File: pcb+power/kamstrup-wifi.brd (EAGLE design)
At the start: 36 x 81.3 mm, 23 parts, among them T1 BT137, T2 BT137

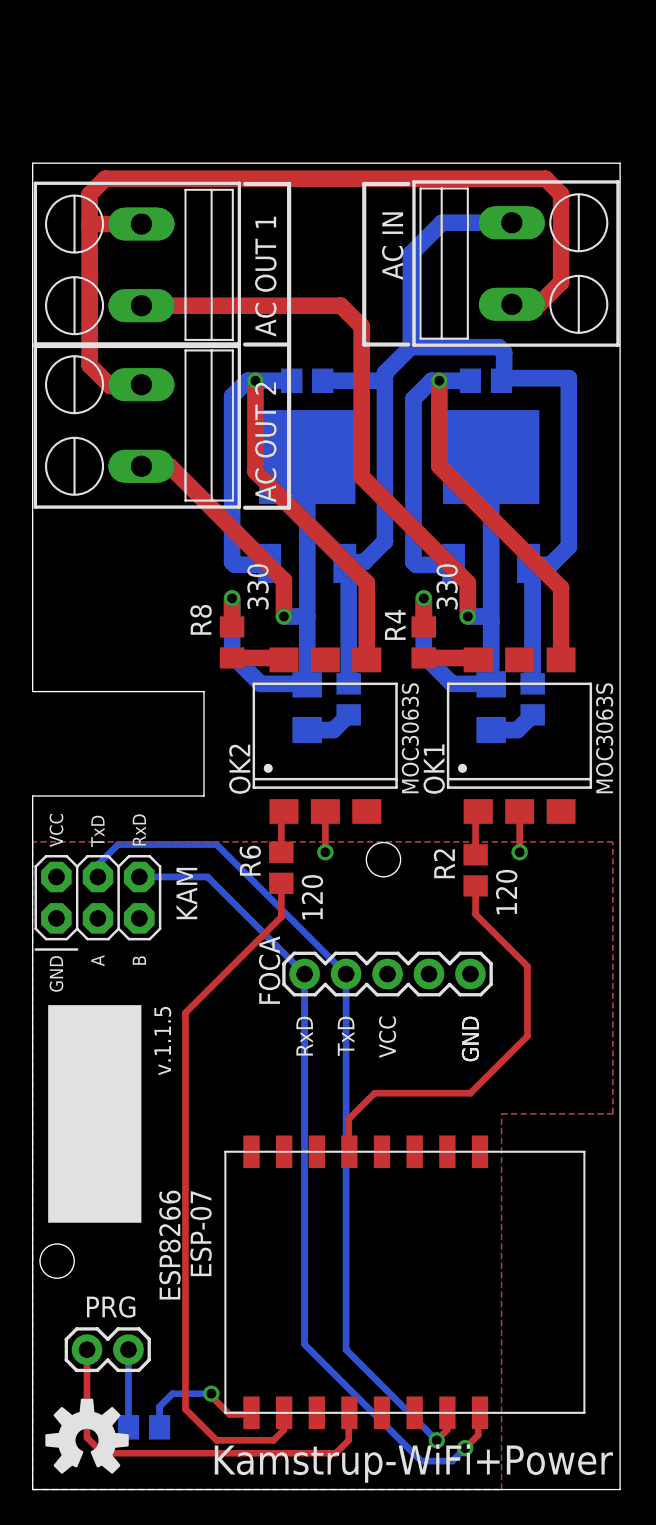
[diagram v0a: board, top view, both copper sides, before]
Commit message: v.1.2.1
+ watchdog and pulldown on gpio 15
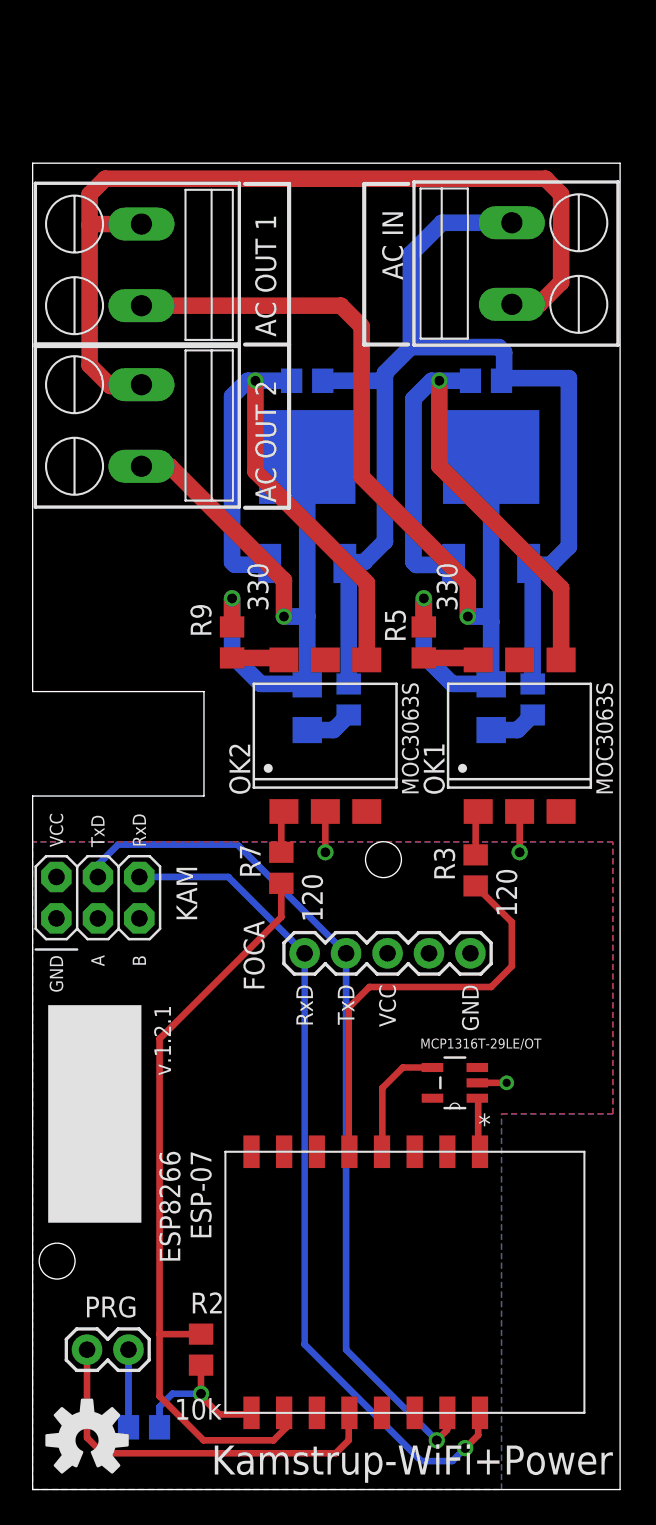
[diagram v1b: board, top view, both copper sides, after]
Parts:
- added R10: 39, rcl:R0805
- added U2: MCP1316T-29LE/OT, Microchip_By_element14_Batch_1:SOT95P270X145-5N
- R2: value 120 -> 10k
- R3, R7: value 330 -> 120
- R5, R9: value 39 -> 330
- R6: value 120 -> 39
- moved R2 33.8 mm to (10.3, 8.57)
- moved R3 30.0 mm to (27.1, 37.9), flipped to the top, turned to 90 degrees
- moved R7 29.9 mm to (15.2, 38.1), flipped to the top, turned to 90 degrees
- moved R6 18.5 mm to (30.6, 48.4), flipped to the bottom, turned to 270 degrees
- moved R8 16.7 mm to (16.8, 67.9), flipped to the bottom, turned to 180 degrees
- moved R4 16.5 mm to (27.8, 67.9), flipped to the bottom, turned to 180 degrees
- moved R9 7.95 mm to (12.2, 51.9), flipped to the top, turned to 90 degrees
- moved R5 7.53 mm to (24.0, 51.9), flipped to the top, turned to 90 degrees
- moved FOCA 1.27 mm to (16.7, 32.9)
- renumbered U$1 to U1
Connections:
- new net N$19: U1.REST, U2.1
- new net N$20: U1.GPIO16, U2.4
- net 3.3V: now also U2.5
- net GND: now also R2.1, U2.2
- net N$10: now also R10.2; no longer R9.2
- net N$11: now also R3.1; no longer R2.1
- net N$12: now also R3.2; no longer R2.2
- net N$13: now also R4.1; no longer R3.1
- net N$14: now also R5.1; no longer R4.1
- net N$15: now also R5.2; no longer R4.2
- net N$16: now also R2.2, R7.1; no longer R6.1
- net N$17: now also R6.2; no longer R5.2
- net N$5: now also R7.2; no longer R6.2
- net N$6: now also R8.1; no longer R7.1
- net N$7: now also R9.1; no longer R8.1
- net N$8: now also R9.2; no longer R8.2
- net N$9: now also R10.1, R4.2, R6.1, R8.2; no longer R3.2, R5.1, R7.2, R9.1
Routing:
- net N$20: track 0.00 -> 7.51 mm
- net N$16: track 42.8 -> 47.3 mm
- net GND: track 14.2 -> 17.8 mm, vias 3 -> 4
- net N$19: track 0.00 -> 3.35 mm
- net N$2: track 52.6 -> 53.3 mm
- net N$1: track 51.0 -> 51.7 mm
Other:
- board text added: "Part RS# C1, C2 766-1150 JP1, JP2, JP3 821-8701 KAM 702-2937 OK1, OK2 691-2319 R1, R2 721-7820 R3, R7 721-6867 R4, R5, R8, R9 770-8742 R6, R10 770-8798 T1, T2 792-0709"
- board text added: "v.1.2.1"
- board text removed: "Part RS# C1, C2 766-1150 JP1, JP2, JP3 821-8701 KAM 702-2937 OK1, OK2 691-2319 R1 721-7820 R2, R6 721-6867 R3, R4, R7, R8 770-8742 R5, R9 770-8798 T1, T2 792-0709"
- board text removed: "v.1.1.5"

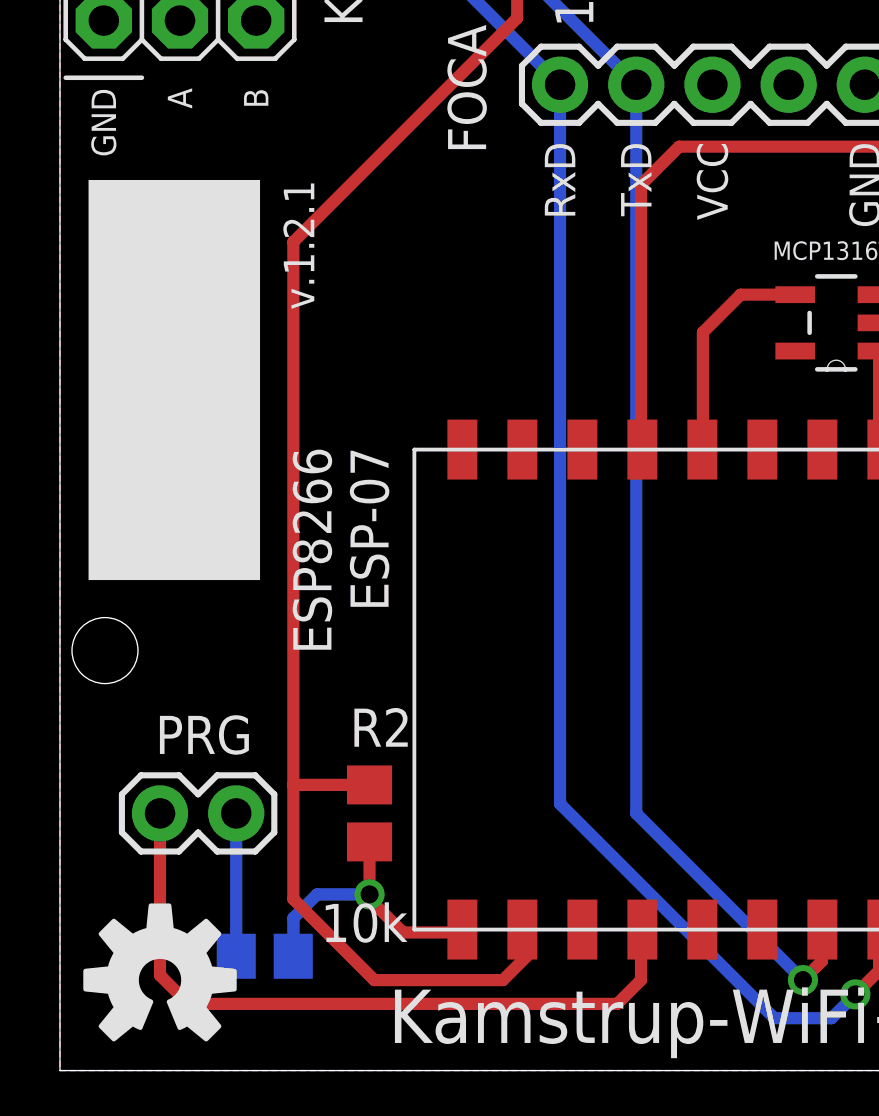
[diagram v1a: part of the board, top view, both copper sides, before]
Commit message: added pull up resistor on GPIO02
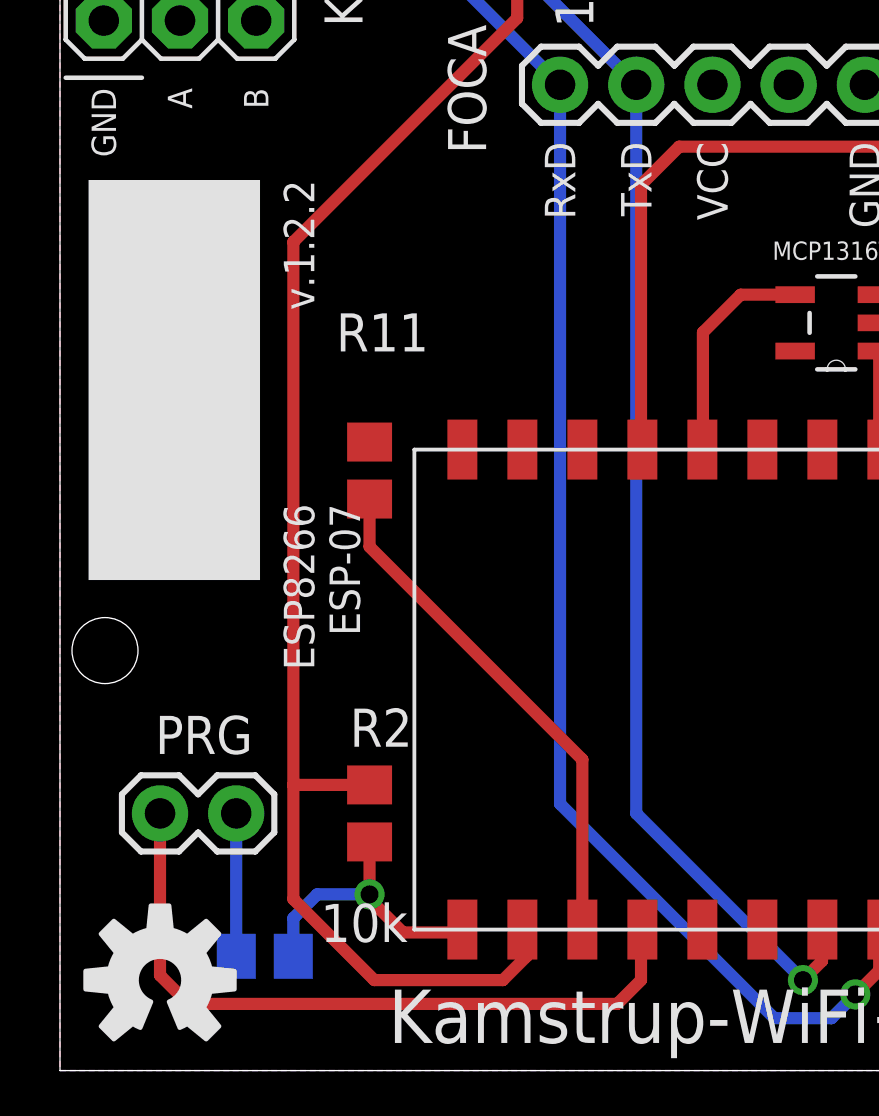
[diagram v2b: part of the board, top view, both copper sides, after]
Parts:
- added R11: 10k, rcl:R0805
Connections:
- new net N$21: R11.2, U1.GPIO2
- net 3.3V: now also R11.1
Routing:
- net N$21: track 0.00 -> 17.3 mm
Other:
- board text added: "Part RS# C1, C2 766-1150 JP1, JP2, JP3 821-8701 KAM 702-2937 OK1, OK2 691-2319 R1, R2, R11 721-7820 R3, R7 721-6867 R4, R5, R8, R9 770-8742 R6, R10 770-8798 T1, T2 792-0709"
- board text added: "v.1.2.2"
- board text removed: "Part RS# C1, C2 766-1150 JP1, JP2, JP3 821-8701 KAM 702-2937 OK1, OK2 691-2319 R1, R2 721-7820 R3, R7 721-6867 R4, R5, R8, R9 770-8742 R6, R10 770-8798 T1, T2 792-0709"
- board text removed: "v.1.2.1"
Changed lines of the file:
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@@
 <?xml version="1.0" encoding="utf-8"?>
 <!DOCTYPE eagle SYSTEM "eagle.dtd">
-<eagle version="7.2.0">
+<eagle version="7.6.0">
 <drawing>
 <settings>
@@
 <setting verticaltext="up"/>
 </settings>
-<grid distance="0.00625" unitdist="inch" unit="mm" style="dots" multiple="1" display="no" altdistance="0.0125" altunitdist="inch" altunit="mm"/>
+<grid distance="0.00625" unitdist="inch" unit="inch" style="dots" multiple="1" display="no" altdistance="0.0125" altunitdist="inch" altunit="inch"/>
 <layers>
 <layer number="1" name="Top" color="4" fill="1" visible="yes" active="yes"/>
@@
 <text x="19.20875" y="30.95625" size="1.016" layer="25" rot="R90" align="center-right">TxD</text>
 <text x="16.66875" y="30.95625" size="1.016" layer="25" rot="R90" align="center-right">RxD</text>
-<text x="7.77875" y="20.79625" size="1.27" layer="25" ratio="10" rot="R270">ESP8266
+<text x="7.46125" y="18.89125" size="1.016" layer="25" ratio="10" rot="R270">ESP8266
 ESP-07</text>
-<text x="7.46125" y="29.68625" size="1.016" layer="25" ratio="15" rot="R270">v.1.2.1</text>
+<text x="7.46125" y="29.68625" size="1.016" layer="25" ratio="15" rot="R270">v.1.2.2</text>
 <text x="26.82875" y="30.95625" size="1.016" layer="25" rot="R90" align="center-right">GND</text>
 <text x="22.06625" y="78.4225" size="1.27" layer="25" ratio="20" rot="R90" align="center-right">AC IN</text>
@@
 KAM             702-2937
 OK1, OK2        691-2319
-R1, R2          721-7820
+R1, R2, R11     721-7820
 R3, R7          721-6867
 R4, R5, R8, R9  770-8742
@@
 <attribute name="VALUE" x="11.58875" y="5.55625" size="1.27" layer="25" rot="R180"/>
 </element>
+<element name="R11" library="rcl" package="R0805" value="10k" x="10.31875" y="20.0025" smashed="yes" rot="R270">
+<attribute name="NAME" x="9.2075" y="23.97125" size="1.27" layer="25"/>
+<attribute name="VALUE" x="9.36625" y="22.38375" size="1.27" layer="27"/>
+</element>
 </elements>
 <signals>
@@
 <contactref element="U1" pad="VCC"/>
 <contactref element="U2" pad="5"/>
+<contactref element="R11" pad="1"/>
 </signal>
 <signal name="N$1">
@@
 <wire x1="21.43125" y1="20.71875" x2="21.4125" y2="20.7" width="0.4064" layer="1"/>
 </signal>
+<signal name="N$21">
+<contactref element="R11" pad="2"/>
+<contactref element="U1" pad="GPIO2"/>
+<wire x1="17.4125" y1="4.7" x2="17.4125" y2="10.36875" width="0.4064" layer="1"/>
+<wire x1="17.4125" y1="10.36875" x2="10.31875" y2="17.4625" width="0.4064" layer="1"/>
+<wire x1="10.31875" y1="17.4625" x2="10.31875" y2="19.0525" width="0.4064" layer="1"/>
+</signal>
 </signals>

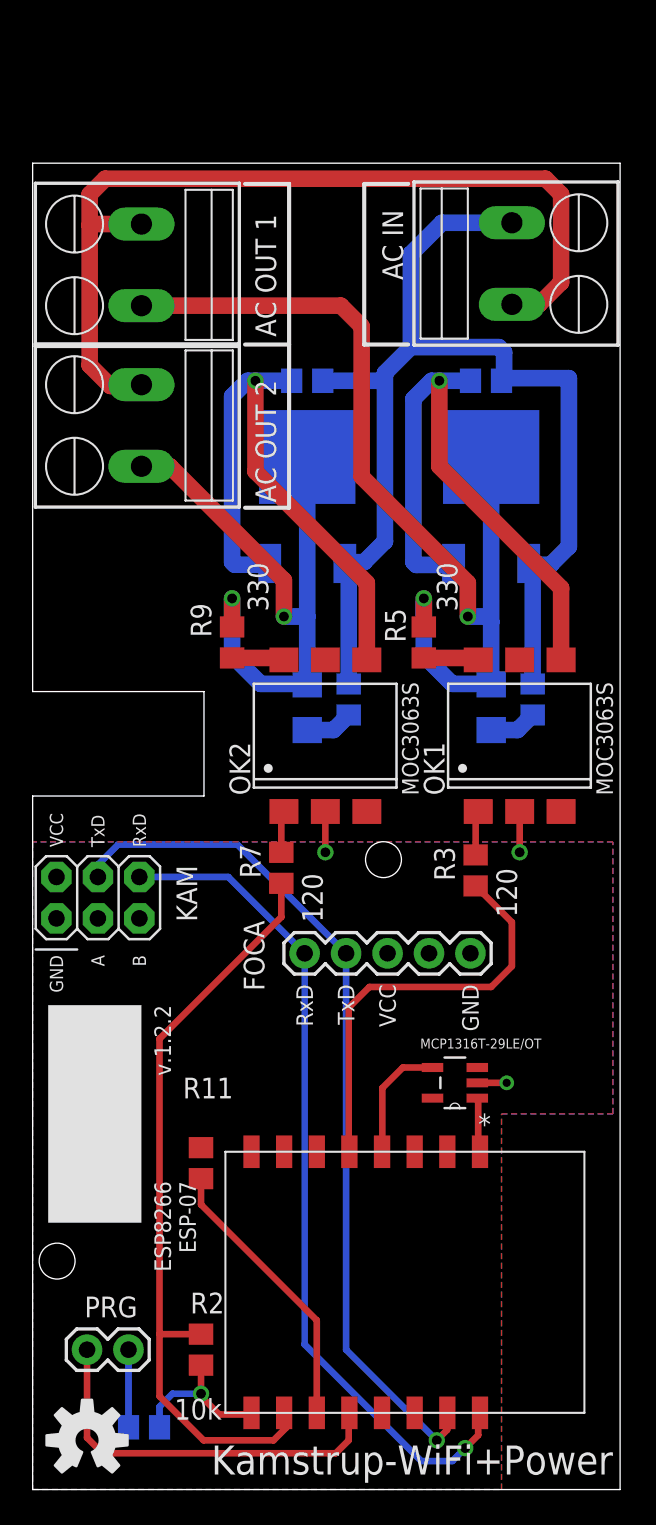
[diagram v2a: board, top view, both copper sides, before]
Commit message: Labels for N and L on AC in/out
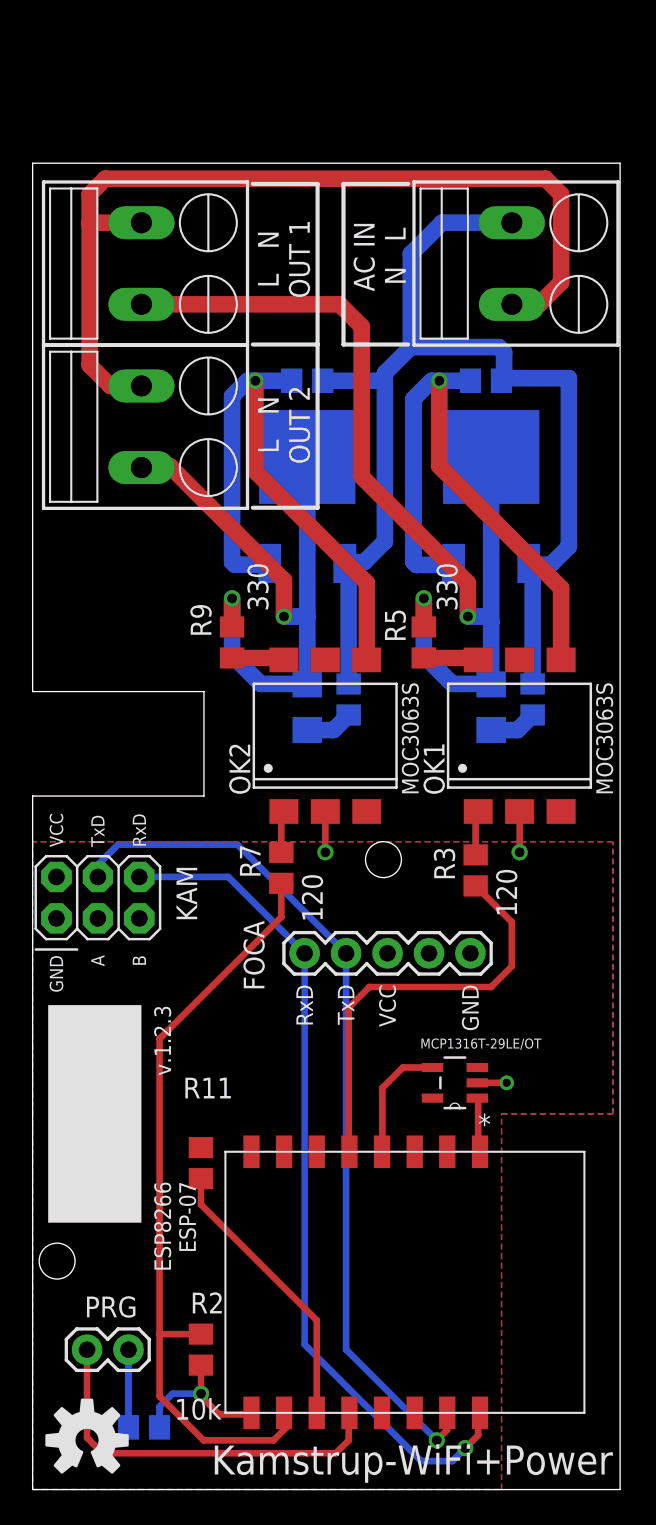
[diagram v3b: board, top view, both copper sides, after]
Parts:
- moved JP2 5.08 mm to (6.67, 77.6), turned to 270 degrees
- moved JP3 4.92 mm to (6.67, 67.6), turned to 270 degrees
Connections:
- net N$15: now also JP2.2; no longer JP2.1
- net N$18: now also JP2.1, JP3.1; no longer JP2.2, JP3.2
- net N$8: now also JP3.2; no longer JP3.1
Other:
- board text added: "AC IN N L"
- board text added: "L N OUT 1"
- board text added: "L N OUT 2"
- board text added: "v.1.2.3"
- board text removed: "AC IN"
- board text removed: "AC OUT 1"
- board text removed: "AC OUT 2"
- board text removed: "v.1.2.2"
